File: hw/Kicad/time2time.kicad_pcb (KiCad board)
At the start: 2 copper layers, 50 x 70 mm, 97 parts, among them J201 USB_B_Micro, J202 LIPO 1S, J301 Conn_display, J302 Conn_expansion, J303 Conn_E3Z-D62, Q301 TSM2312CX, SW1 SW_SPDT, SW301 SW_Push, SW302 SW_Push, SW303 SW_Push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

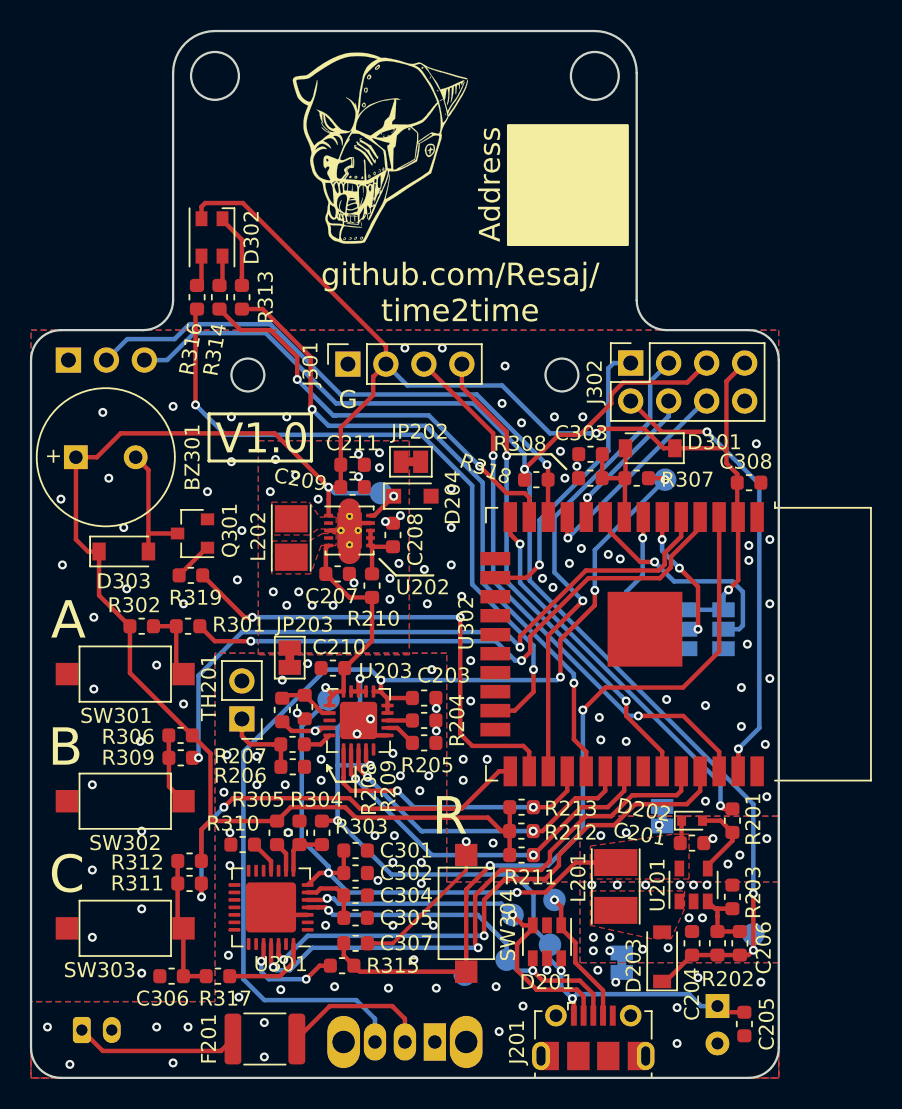
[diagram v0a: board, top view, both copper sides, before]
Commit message: V1.1 version. UART fixed and some signals renamed
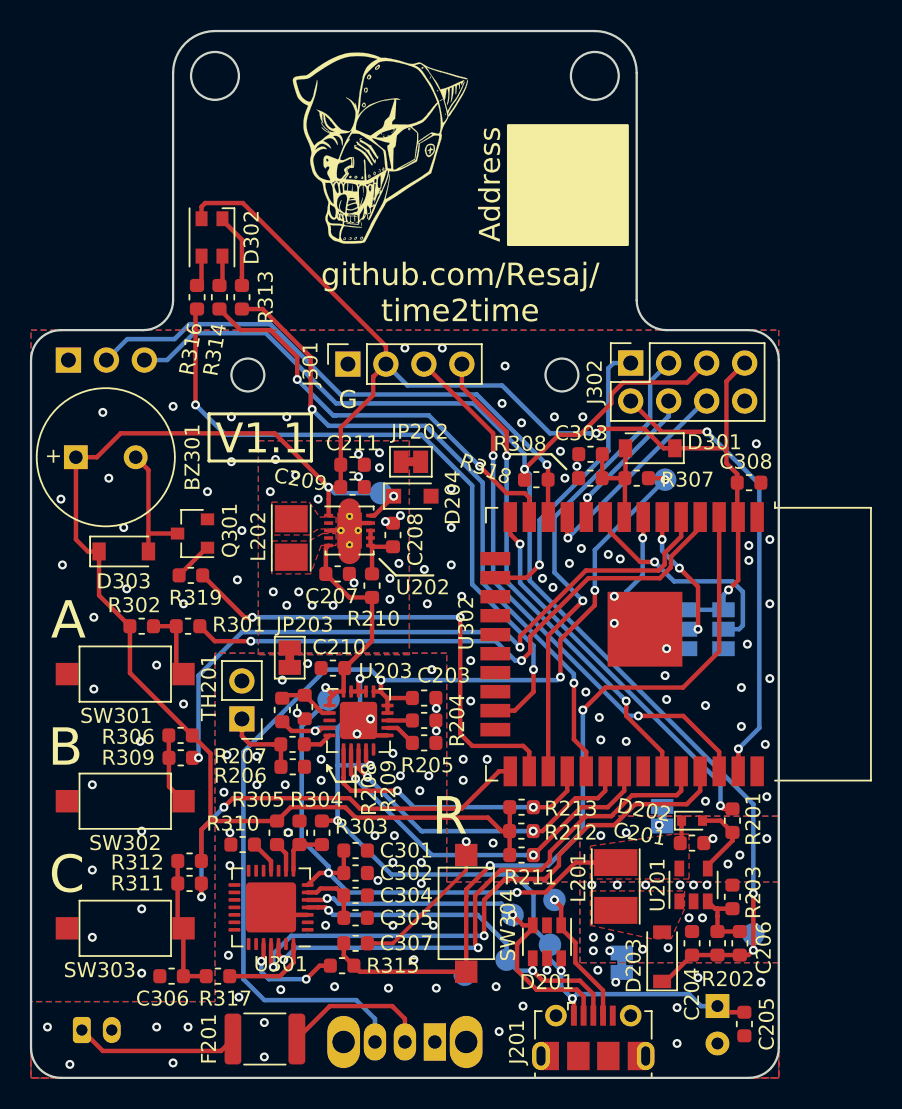
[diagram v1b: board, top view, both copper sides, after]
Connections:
- net /microcontroller/BUZZER renamed /microcontroller/BUZZER_PWM
- net /microcontroller/SLEEP renamed /microcontroller/SLEEP_12V
- R211 pad 2: /microcontroller/PW_STATE3 -> /microcontroller/PW_STATE2
- R212 pad 2: /microcontroller/PW_STATE2 -> /microcontroller/PW_STATE1
- U203 pad 7: /microcontroller/PW_STATE3 -> /microcontroller/PW_STATE2
- U203 pad 8: /microcontroller/PW_STATE2 -> /microcontroller/PW_STATE1
- U301 pad 25: /microcontroller/RX -> /microcontroller/UART_TX
- U301 pad 26: /microcontroller/TX -> /microcontroller/UART_RX
- U302 pad 30: /microcontroller/PW_STATE2 -> /microcontroller/PW_STATE1
- U302 pad 31: /microcontroller/PW_STATE3 -> /microcontroller/PW_STATE2
- U302 pad 34: /microcontroller/RX -> /microcontroller/UART_RX
- U302 pad 35: /microcontroller/TX -> /microcontroller/UART_TX
- U302 pad 39: (no net) -> GNDS
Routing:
- net /microcontroller/UART_TX: track 0.00 -> 38.7 mm, vias 0 -> 2
- net /microcontroller/RX: track 37.9 -> 0.00 mm, vias 2 -> 0
- net /microcontroller/TX: track 36.8 -> 0.00 mm, vias 2 -> 0
- net /microcontroller/UART_RX: track 0.00 -> 36.4 mm, vias 0 -> 2
- net /microcontroller/PW_STATE3: track 25.2 -> 0.00 mm, vias 2 -> 0
- net /microcontroller/PW_STATE1: track 0.00 -> 21.9 mm, vias 0 -> 2
- net /microcontroller/PW_STATE2: track 21.9 -> 25.2 mm
- net GNDS: vias 71 -> 76
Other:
- board text added: "V1.1"
- board text added: "time2time project - V1.1 Designed by Resaj Puma Pride Robotics Team"
- board text removed: "V1.0"
- board text removed: "time2time project - V1.0 Designed by Resaj Puma Pride Robotics Team"

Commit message: Resistor value changed for ADC battery monitor
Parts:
- R307: value 33K -> 47K
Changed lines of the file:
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@@
       (effects (font (size 1 1) (thickness 0.15)))
     )
-    (fp_text value 33K (at 0 1.43 180) (layer F.Fab)
+    (fp_text value 47K (at 0 1.43 180) (layer F.Fab)
       (effects (font (size 1 1) (thickness 0.15)))
     )

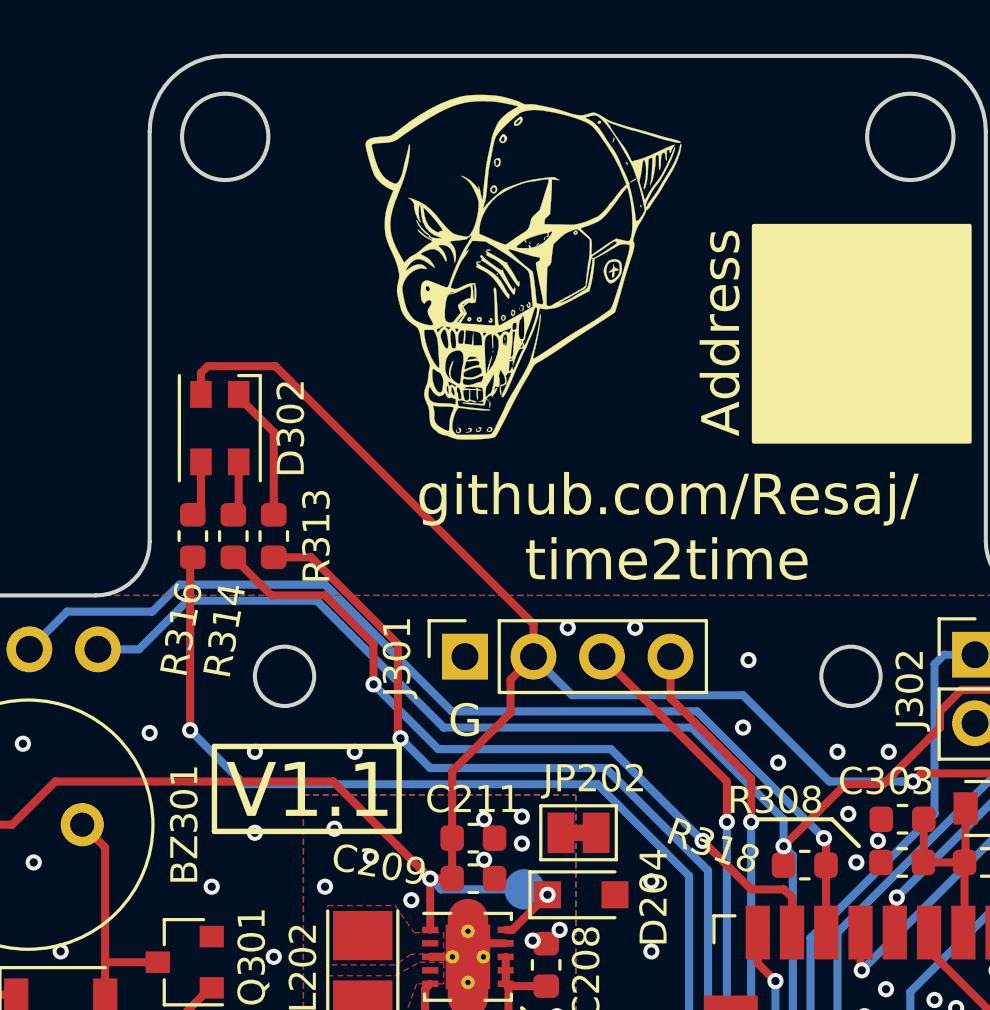
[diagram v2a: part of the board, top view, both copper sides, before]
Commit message: t2t_fw. Add schottky diode to prevent the ESP32 sensor pin from exced 3V3
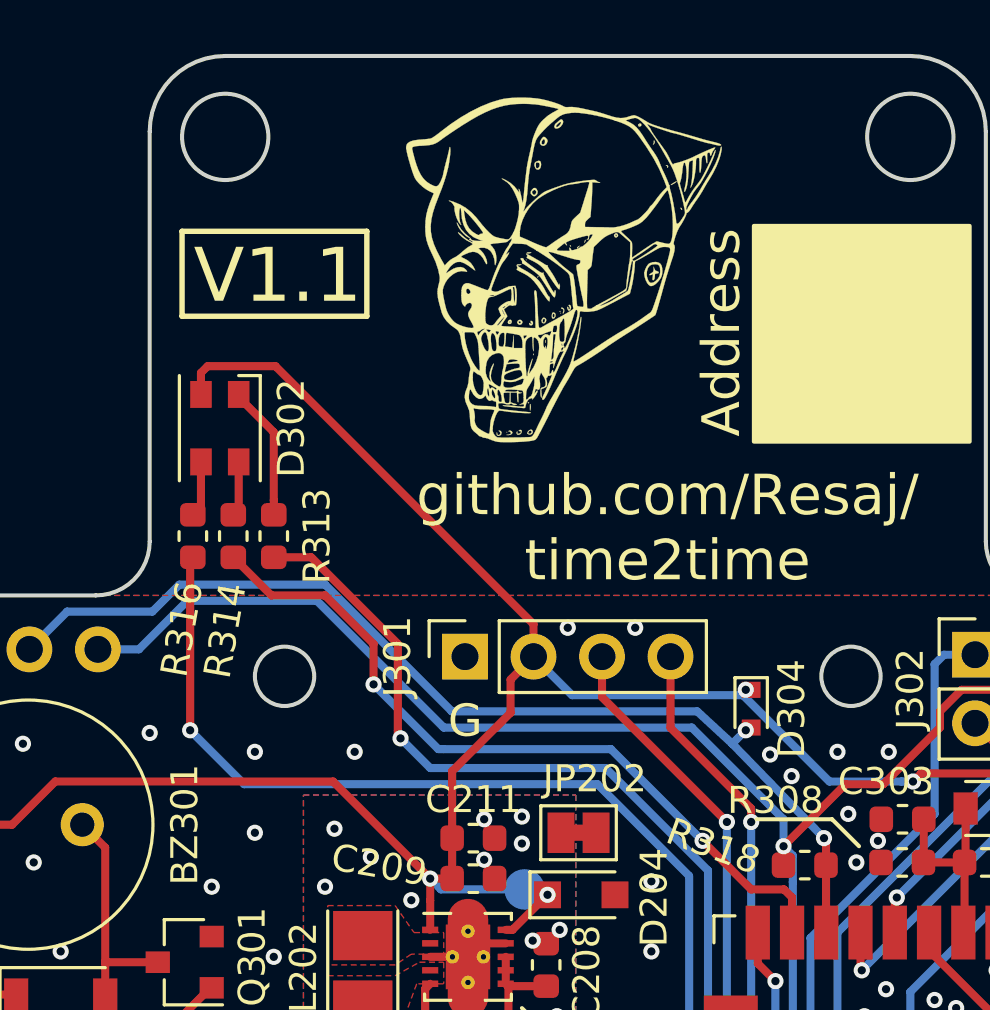
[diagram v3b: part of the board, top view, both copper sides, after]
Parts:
- removed the ? at (148.4, 62.4)
- removed the ? at (134.5, 109.5)
- added ?: , time2time:logo_PumaPride_14x14, F.Cu at (149.9, 62.5)
- added D304: RB751S40T5G, Diode_SMD:D_SOD-523, F.Cu at (156.8, 79.2)
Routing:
- net /microcontroller/SENSOR: track 37.9 -> 38.8 mm, vias 1 -> 2
- net +3V3: track 160.1 -> 160.6 mm, vias 4 -> 5
- net GNDS: vias 76 -> 75
